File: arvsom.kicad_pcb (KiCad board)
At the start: 12 copper layers, 55 x 40 mm, 413 parts, among them J1 TAG-10PIN, J3 DF40C-100DP-0.4V(51), J4 DF40C-100DP-0.4V(51), Q1 DMG1013UWQ-7, Q5 DMG1012UW, U1 MT53D1024M32D4DT-053, U10 TDA19988BHN_C1,557, U11 KSZ9031RNXCA, U13 VIC7100, U2 GD25LQ256DWIGR, U3 MT53D1024M32D4DT-053, U4 CSD86330Q3D, U5 LMR62014XMF_NOPB, U6 CSD86330Q3D, U7 STM811RW16F, U8 TPS65086100, Y1 ABM8G-25.000MHZ-18-D2Y-T, Y2 ABM8G-25.000MHZ-18-D2Y-T, Y3 ABM8G-27.000MHZ-18-D2Y-T

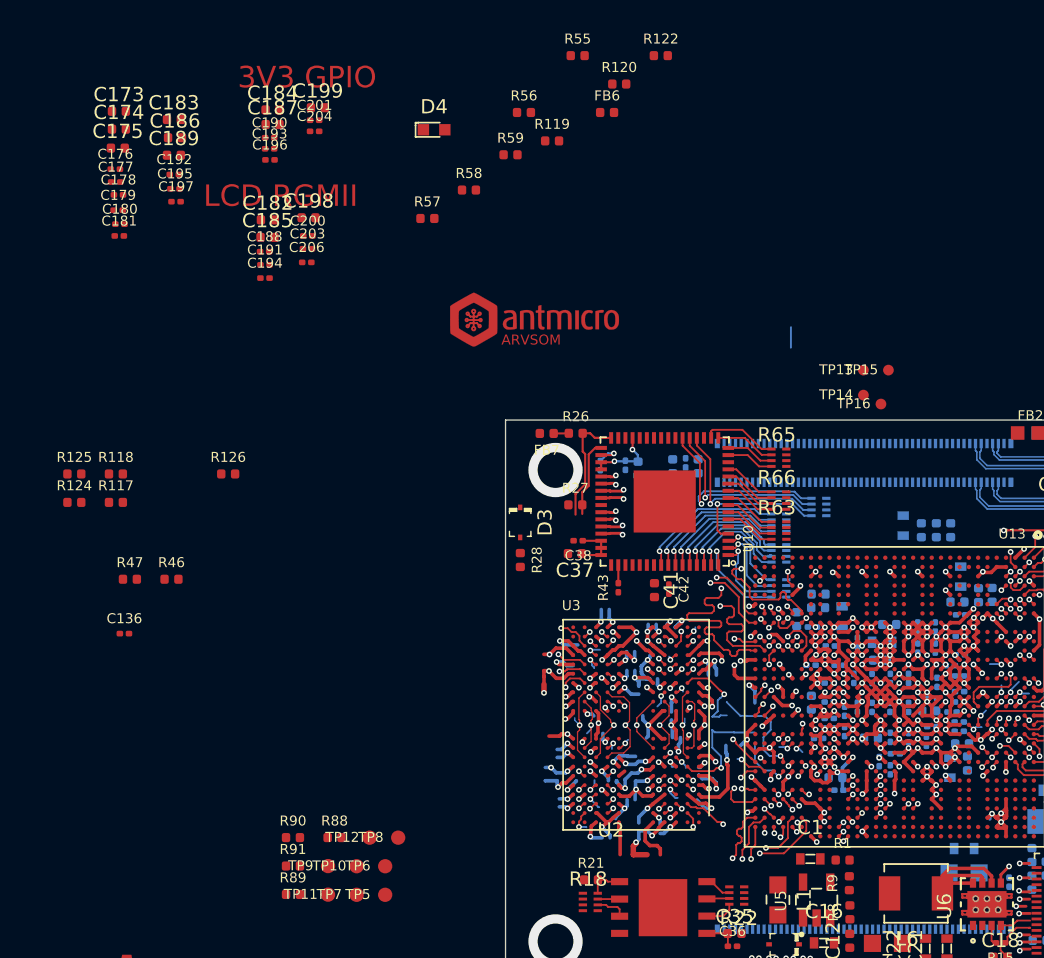
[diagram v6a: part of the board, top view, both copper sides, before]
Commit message: Updated component placement - VIC interfaces decoupling done
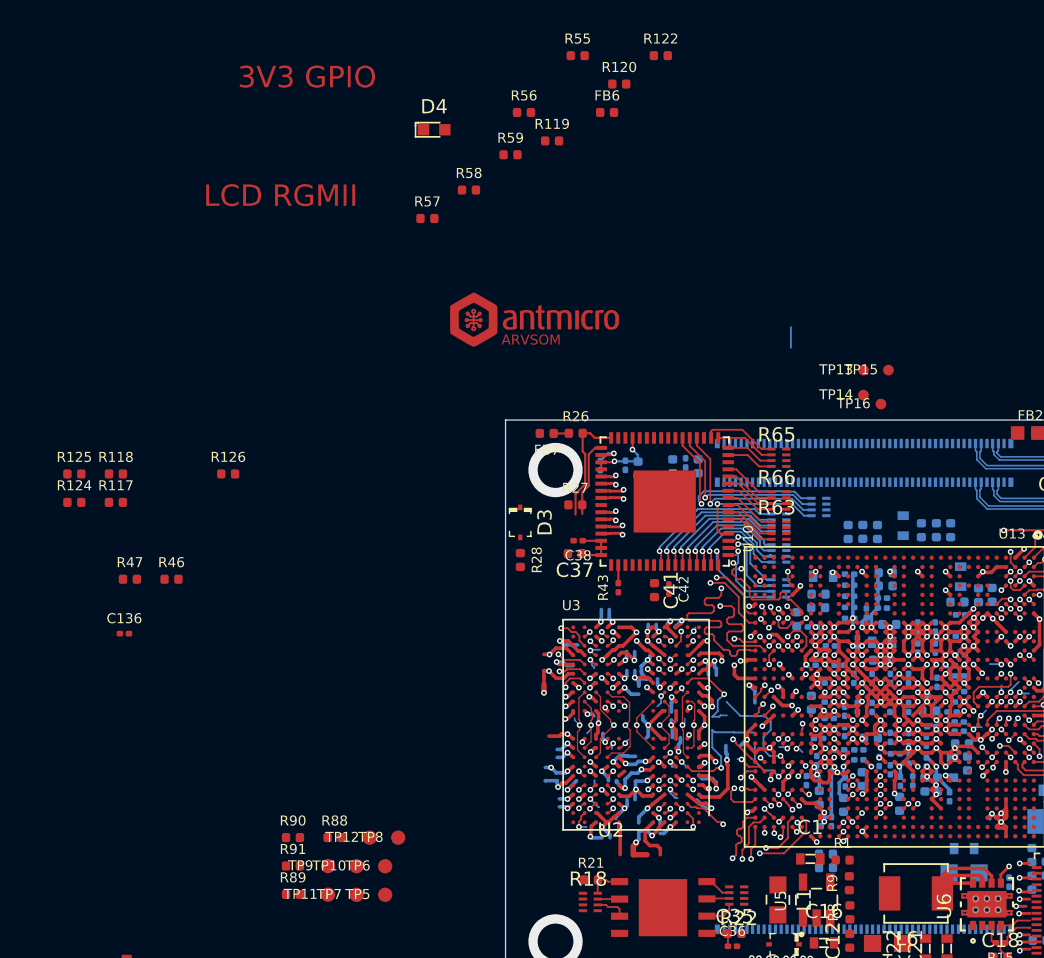
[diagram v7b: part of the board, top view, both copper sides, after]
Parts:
- C173, C174, C175, C176, C177, C178, C179, C180, C181, C182, C183, C184, C185, C186, C187, C188, C189, C190, C191, C192, C193, C194, C195, C196, C197, C198, C199, C200, C201, C203, C204, C206: moved to B.Cu
- moved C173 74.2 mm to (160.3, 80.5), turned to 270 degrees
- moved C176 73.1 mm to (161.1, 81.3), turned to 270 degrees
- moved C174 72.2 mm to (157.6, 81.8), turned to 270 degrees
- moved C177 69.8 mm to (159.5, 78.9), turned to 270 degrees
- moved C183 68.8 mm to (152.5, 85.4), turned to 180 degrees
- moved C189 68.6 mm to (159.4, 80.5), turned to 270 degrees
- moved C186 68.5 mm to (152.5, 86.3), turned to 180 degrees
- moved C178 68.0 mm to (158.3, 78.7), turned to 90 degrees
- moved C179 67.8 mm to (157.7, 80.3), turned to 270 degrees
- moved C175 66.9 mm to (152.0, 81.4), turned to 270 degrees
- moved C192 66.9 mm to (158.5, 80.2), turned to 270 degrees
- moved C195 63.8 mm to (152.8, 83.1), turned to 270 degrees
- moved C197 62.6 mm to (152.1, 83.1), turned to 270 degrees
- moved C180 61.6 mm to (151.8, 78.8), turned to 90 degrees
- moved C181 61.4 mm to (151.1, 80.2), turned to 270 degrees
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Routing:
- net VCC_3V3: track 25.5 -> 34.5 mm
- net VCC_1V8: track 55.2 -> 62.6 mm
- net VCC_0V9: track 41.0 -> 45.3 mm
